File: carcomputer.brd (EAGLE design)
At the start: 112.7 x 94.9 mm, 78 parts, among them IC1 LM358N, K1 351, K2 RT184012, K3 RT184012, Q1 BS170, Q5 TIP136, T1 BC618, T2 BC618, T3 BC618, T4 BC618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

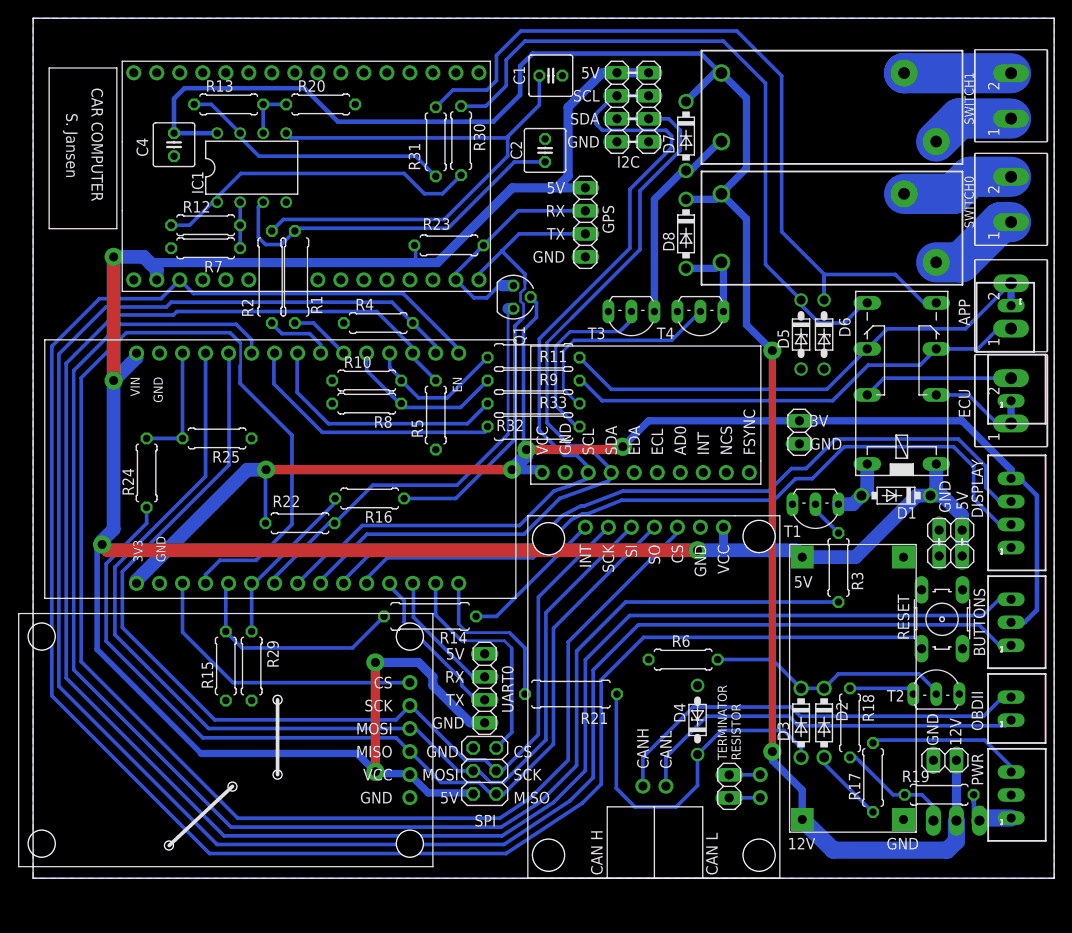
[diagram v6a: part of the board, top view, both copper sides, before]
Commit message: Fixed SD module length. Refitted SPI and I2C header.
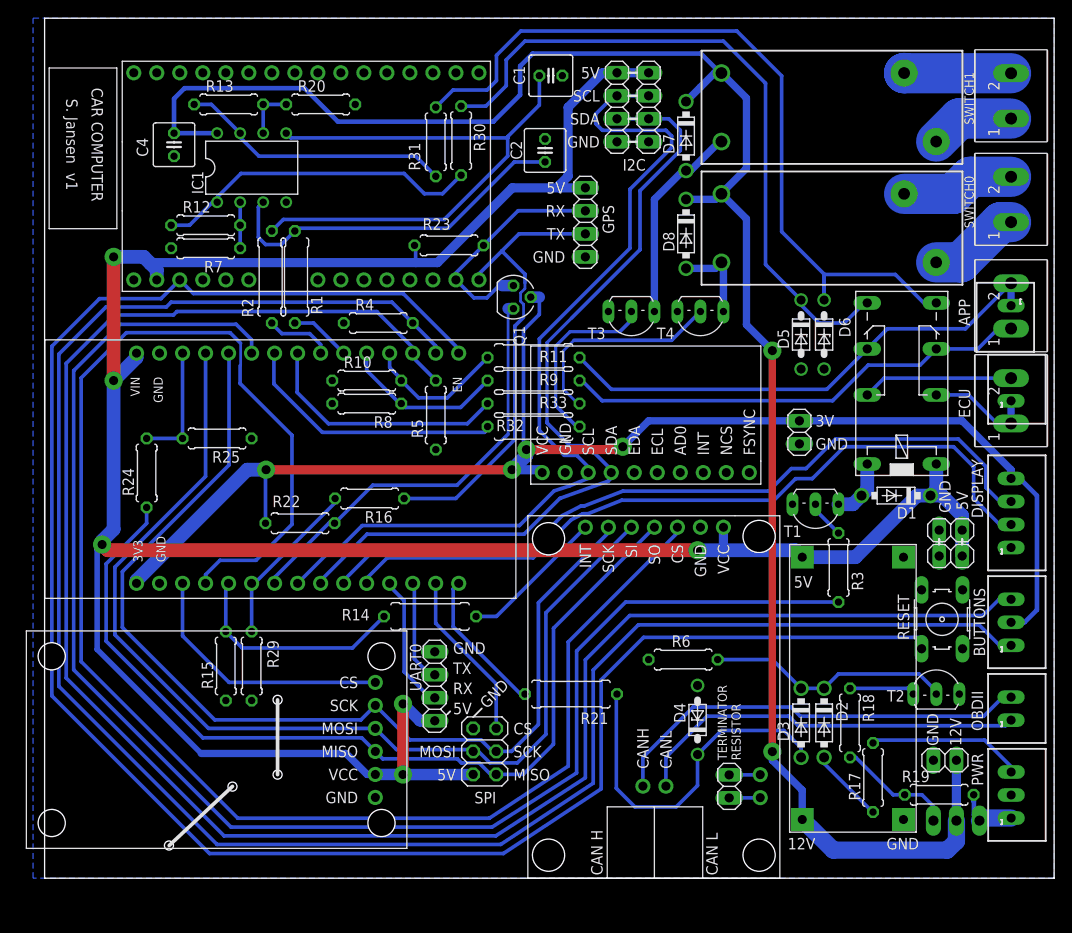
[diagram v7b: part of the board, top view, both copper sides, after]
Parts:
- U$5: value HKD-MICRO-SD-BREAKOUT -> HKD-MICRO-SD-BREAKOUTH
- moved JP_UART0 5.52 mm to (33.2, 14.8)
- moved JP_SPI_1 2.16 mm to (38.7, 7.65)
- moved U$5 1.67 mm to (9.14, 8.94)
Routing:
- net +5V: track 313.4 -> 297.1 mm
- net SPI_CS_1: track 25.1 -> 18.8 mm
- net SD_CS: track 32.8 -> 29.2 mm
- net UART0_TX: track 14.4 -> 11.4 mm
- net UART0_RX: track 17.8 -> 15.0 mm
- net SPI_SCK: track 116.7 -> 114.3 mm
- net SPI_MOSI: track 118.9 -> 116.7 mm
- net PWR_ENABLE: track 18.0 -> 16.0 mm
- net SPI_MISO_5V: track 103.8 -> 102.0 mm
- net +3V3: track 154.6 -> 155.4 mm
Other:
- board size 112.7 x 94.9 mm -> 111.4 x 94.9 mm
- board text added: "S. Jansen v1"
- board text removed: "S. Jansen"

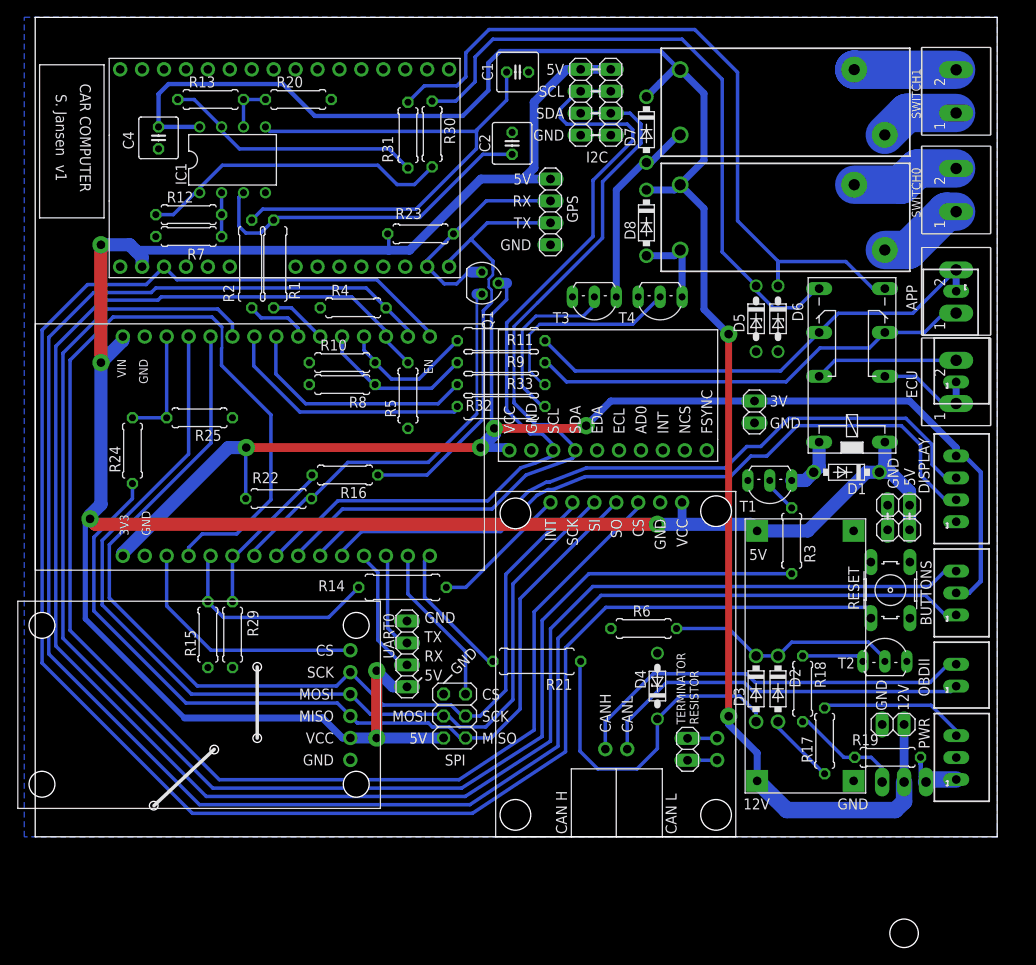
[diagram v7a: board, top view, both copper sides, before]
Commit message: Added connector for fuse. Added extra safety boundries around high voltage areas.
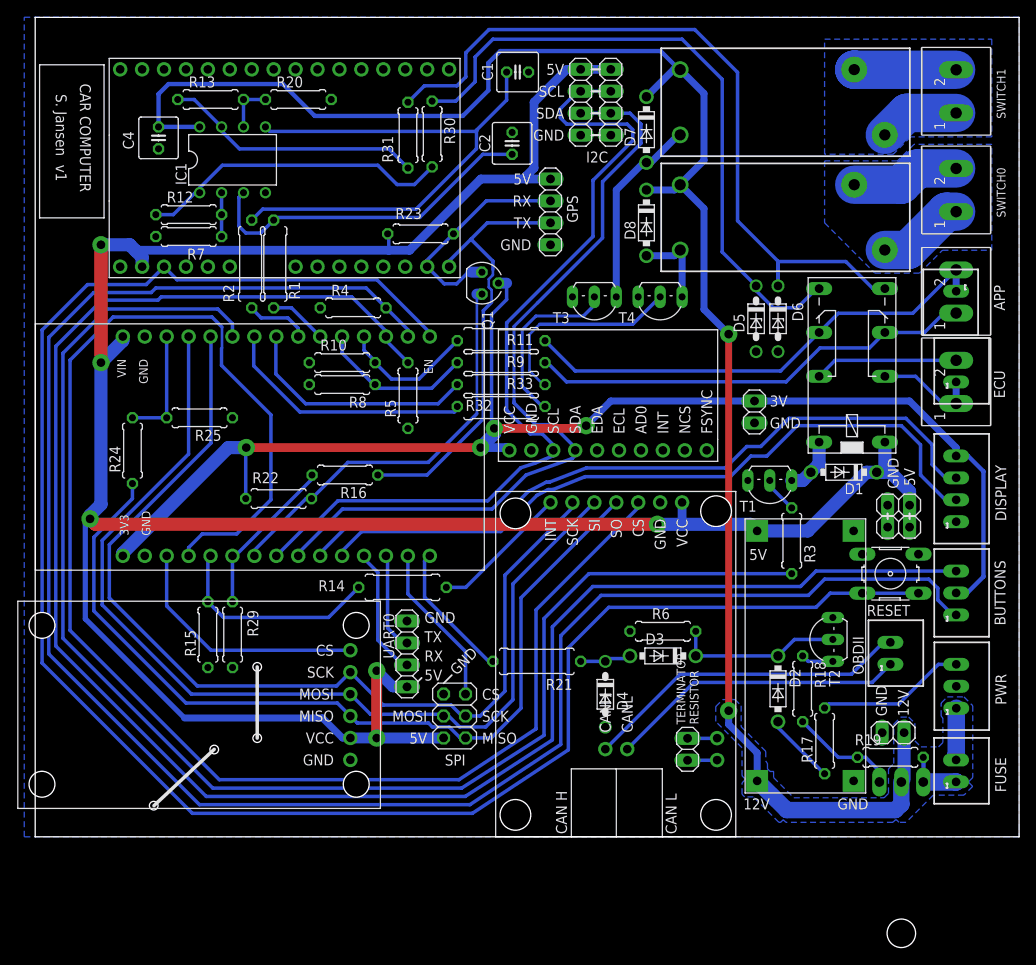
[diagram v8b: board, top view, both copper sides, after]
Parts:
- added FUSE: 2.52B-ZR, con-jst-custom:B2B-ZR2.5
- moved D3 11.4 mm to (62.9, 14.6), turned to 180 degrees
- moved PWR 8.25 mm to (96.9, 11.1)
- moved OBDII 8.03 mm to (89.2, 14.9)
- moved T2 7.41 mm to (81.3, 16.5), turned to 90 degrees
- moved D4 6.11 mm to (56.2, 10.2), turned to 270 degrees
- moved R6 2.25 mm to (62.9, 17.5)
- moved RESET 1.90 mm to (89.2, 24.1), turned to 0 degrees
- moved JP_PWR_12V 0.95 mm to (89.5, 5.71)
- moved D1 0.32 mm to (83.8, 35.9)
- moved Q5 0.32 mm to (90.5, -6.35)
- moved JP_PWR_5V_1 0.32 mm to (90.2, 29.5)
- moved R19 0.32 mm to (89.2, 2.86)
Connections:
- new net N$21: FUSE.1, Q5.3, R19.2
- net +12V: now also FUSE.2; no longer Q5.3, R19.2
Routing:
- net N$11: track 39.1 -> 5.98 mm
- net CAN_L: track 43.9 -> 34.6 mm
- net CAN_H: track 47.4 -> 38.1 mm
- net N$5: track 27.2 -> 19.5 mm
- net N$21: track 0.00 -> 6.68 mm
- net MCU_RESET: track 210.7 -> 215.5 mm
- net N$15: track 7.25 -> 3.76 mm
- net BTN_0: track 213.3 -> 215.7 mm
- net PWR_IN+: track 202.2 -> 201.3 mm
- net +12V: track 6.75 -> 6.00 mm
- net N$14: track 13.0 -> 12.5 mm
- added copper zone on layer 16, net ISO
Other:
- board size 111.4 x 94.9 mm -> 114 x 94.9 mm
